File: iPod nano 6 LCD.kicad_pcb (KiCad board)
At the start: 2 copper layers, 40 x 40 mm, 49 parts, among them J1 Molex_503548-1220, J2 USB_C_Receptacle_USB2.0, J3 Conn_01x06_Male, U1 AP5724, U2. ATSAM3SD8BA-AU, U3 AZ1117-1.8, U4 TPS63001, Y1 32.768k, Y2 20MHz

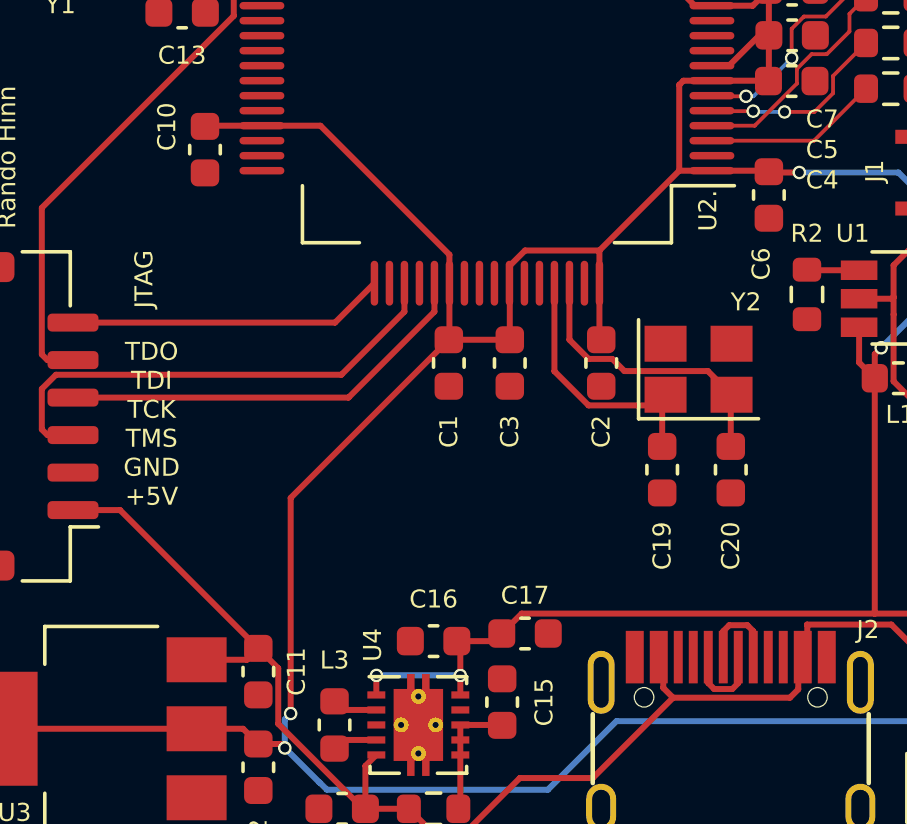
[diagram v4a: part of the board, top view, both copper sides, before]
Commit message: Add Footprint for the flash
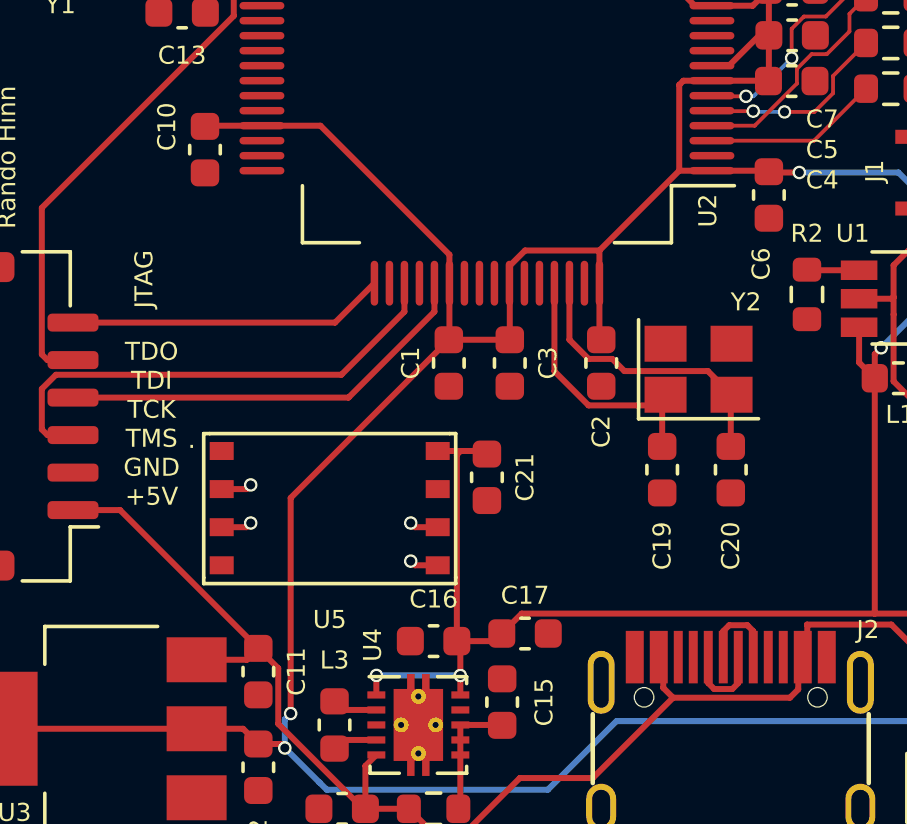
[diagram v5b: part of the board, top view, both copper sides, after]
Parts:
- added C21: 1u, Capacitor_SMD:C_0603_1608Metric, F.Cu at (137.7, 83.8)
- added U5: XTSD04GLGEAG, iPod nano 6 LCD:XTSD04GLGEAG, F.Cu at (132.4, 85.0)
- renumbered U2. to U2
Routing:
- net +3V3: track 40.9 -> 49.0 mm
- net SCLK: track 0.00 -> 1.02 mm, vias 0 -> 1
- net SD_CS: track 0.00 -> 1.02 mm, vias 0 -> 1
- net MISO: track 0.00 -> 0.96 mm, vias 0 -> 1
- net MOSI: track 0.00 -> 0.96 mm, vias 0 -> 1

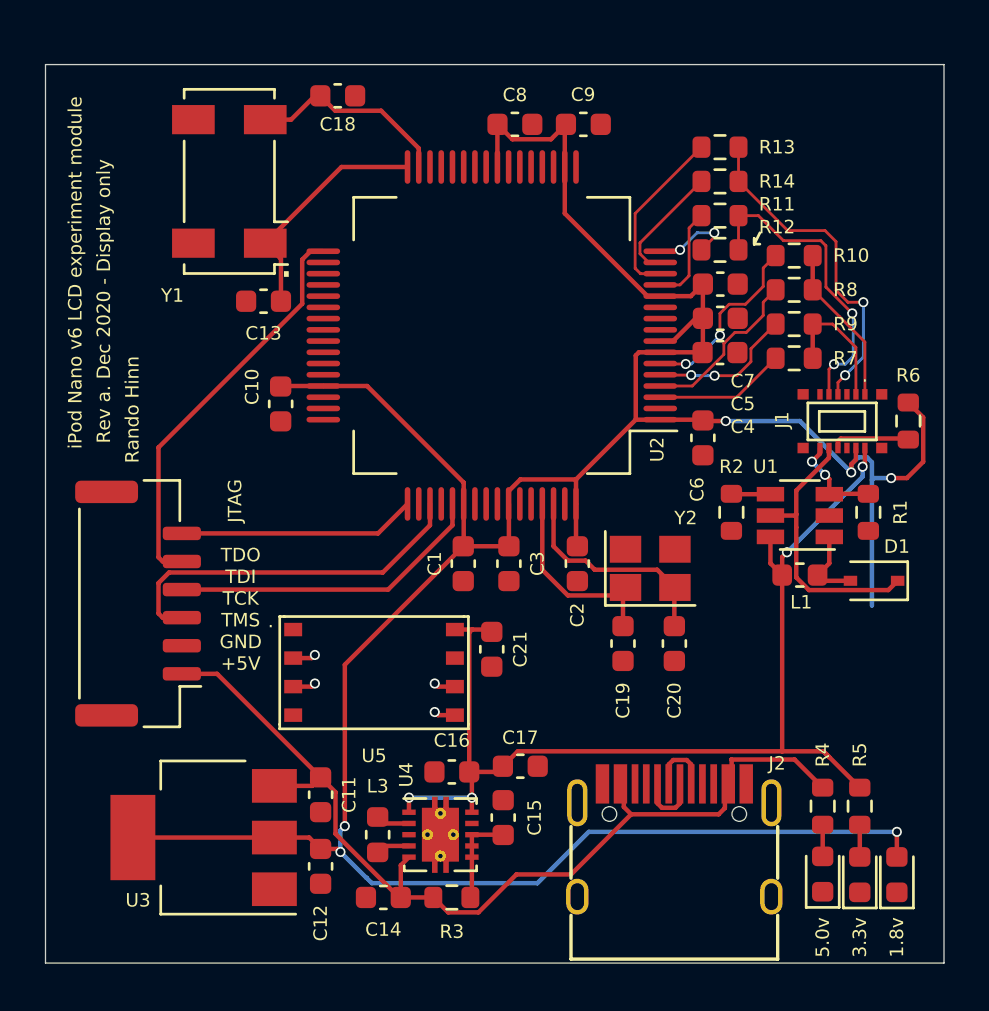
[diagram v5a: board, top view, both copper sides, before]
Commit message: Lets do some routing changes: Unroute all!
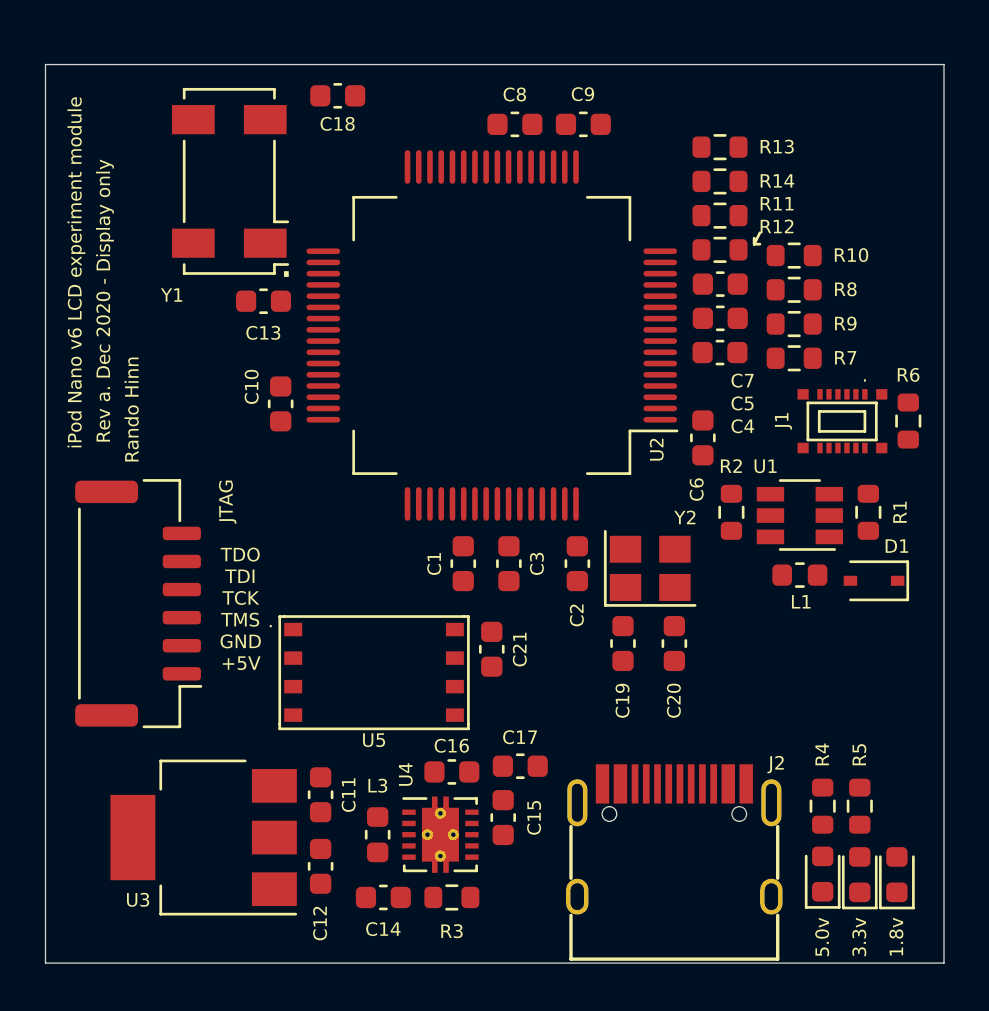
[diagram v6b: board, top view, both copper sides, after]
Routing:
- net VDDIN: track 134.4 -> 0.00 mm, vias 6 -> 0
- net +3V3: track 49.0 -> 0.00 mm, vias 4 -> 0
- net +5V: track 44.0 -> 0.00 mm
- net TDI: track 18.1 -> 0.00 mm
- net TMS: track 16.6 -> 0.00 mm
- net DP: track 15.1 -> 0.00 mm, vias 2 -> 0
- net TCK: track 14.2 -> 0.00 mm
- net DN: track 13.8 -> 0.00 mm, vias 2 -> 0
- net LED+: track 12.5 -> 0.00 mm
- net Net-(C13-Pad1): track 10.6 -> 0.00 mm
- net TDO: track 10.6 -> 0.00 mm
- net Net-(C20-Pad1): track 9.78 -> 0.00 mm
- net Net-(C18-Pad1): track 9.07 -> 0.00 mm
- net Net-(C19-Pad1): track 9.03 -> 0.00 mm
- net Net-(R10-Pad1): track 8.20 -> 0.00 mm, vias 2 -> 0
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
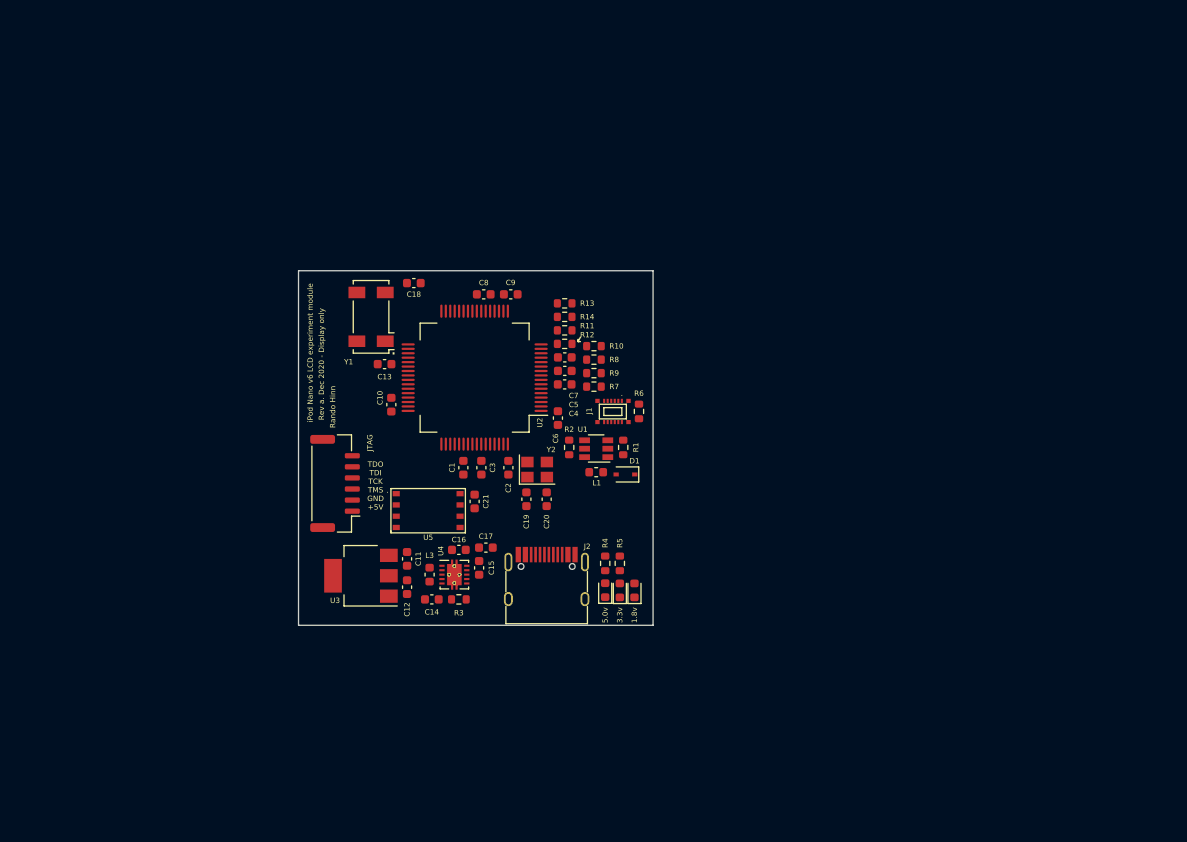
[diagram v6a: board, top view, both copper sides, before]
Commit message: Connecting up the power for the ice40 FPGA I decided to go with.
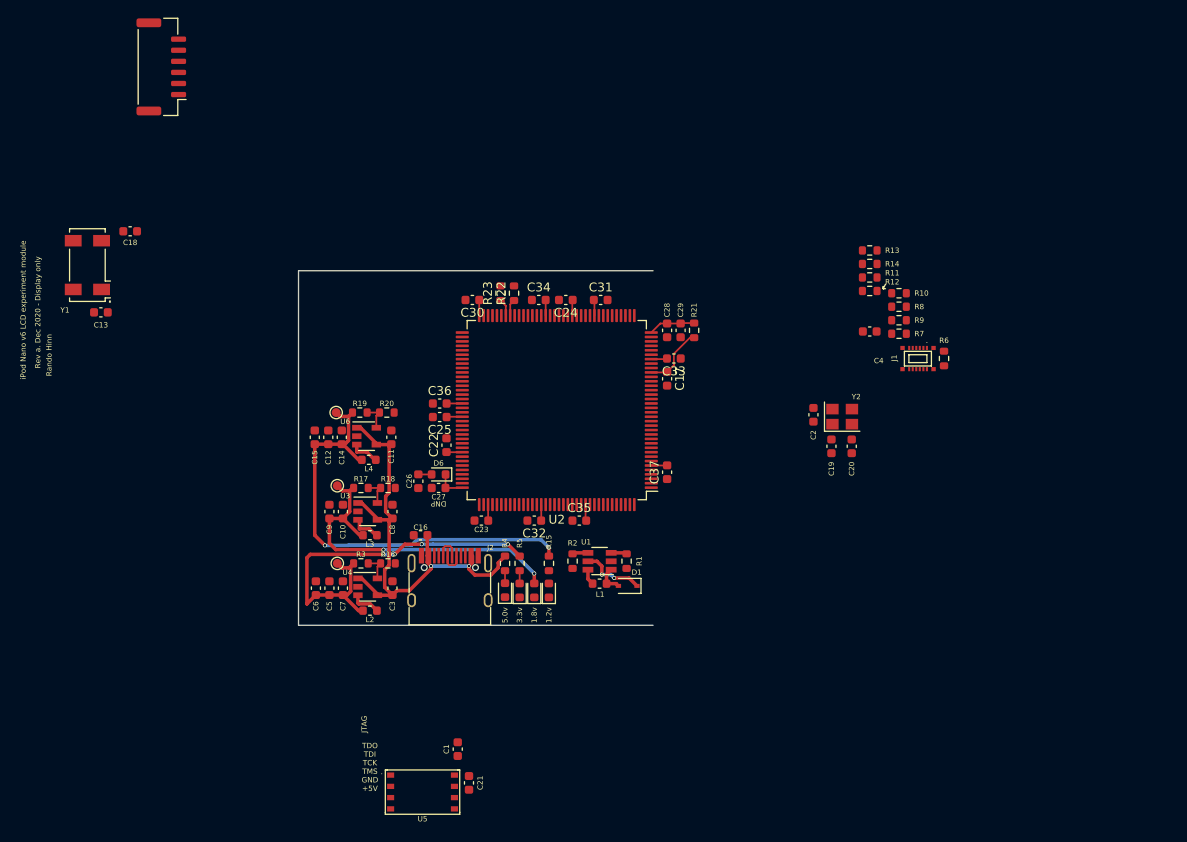
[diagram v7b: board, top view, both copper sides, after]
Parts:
- added C22: 1u, Capacitor_SMD:C_0603_1608Metric, F.Cu at (134.5, 77.5)
- added C23: 1u, Capacitor_SMD:C_0603_1608Metric, F.Cu at (138.4, 86.0)
- added C24: 1u, Capacitor_SMD:C_0603_1608Metric, F.Cu at (148.0, 61.1)
- added C25: 1u, Capacitor_SMD:C_0603_1608Metric, F.Cu at (133.7, 74.3)
- added C26: 1u, Capacitor_SMD:C_0603_1608Metric, F.Cu at (131.3, 81.5)
- added C27: DNP, Capacitor_SMD:C_0603_1608Metric, F.Cu at (133.6, 82.3)
- added C28: 10u, Capacitor_SMD:C_0603_1608Metric, F.Cu at (159.4, 64.5)
- added C29: 100n, Capacitor_SMD:C_0603_1608Metric, F.Cu at (160.9, 64.5)
- added C30: 1u, Capacitor_SMD:C_0603_1608Metric, F.Cu at (137.4, 61.1)
- added C31: 1u, Capacitor_SMD:C_0603_1608Metric, F.Cu at (151.9, 61.1)
- added C32: 1u, Capacitor_SMD:C_0603_1608Metric, F.Cu at (144.4, 86.0)
- added C33: 1u, Capacitor_SMD:C_0603_1608Metric, F.Cu at (160.1, 67.7)
- added C34: 1u, Capacitor_SMD:C_0603_1608Metric, F.Cu at (144.9, 61.1)
- added C35: 1u, Capacitor_SMD:C_0603_1608Metric, F.Cu at (149.5, 86.0)
- added C36: 1u, Capacitor_SMD:C_0603_1608Metric, F.Cu at (133.7, 72.8)
- added C37: 1u, Capacitor_SMD:C_0603_1608Metric, F.Cu at (159.4, 80.5)
- added D5: +3.3v, LED_SMD:LED_0603_1608Metric, F.Cu at (146.1, 93.9)
- added D6: ~~800mVf, Diode_SMD:D_0603_1608Metric, F.Cu at (133.6, 80.8)
- added L2: 2.2u, Inductor_SMD:L_0603_1608Metric, F.Cu at (125.9, 96.1)
- added L4: 2.2u, Inductor_SMD:L_0603_1608Metric, F.Cu at (125.7, 79.1)
- added R15: 8, Resistor_SMD:R_0603_1608Metric, F.Cu at (146.1, 90.8)
- added R16: 100k, Resistor_SMD:R_0603_1608Metric, F.Cu at (127.9, 90.8)
- added R17: 200k, Resistor_SMD:R_0603_1608Metric, F.Cu at (124.8, 82.3)
- added R18: 100k, Resistor_SMD:R_0603_1608Metric, F.Cu at (127.9, 82.3)
- added R19: 100k, Resistor_SMD:R_0603_1608Metric, F.Cu at (124.7, 73.8)
- added R20: 100k, Resistor_SMD:R_0603_1608Metric, F.Cu at (127.8, 73.8)
- added R21: 100, Resistor_SMD:R_0603_1608Metric, F.Cu at (162.4, 64.5)
- added R22: 2k2, Resistor_SMD:R_0603_1608Metric, F.Cu at (142.1, 60.3)
- added R23: 10k, Resistor_SMD:R_0603_1608Metric, F.Cu at (140.6, 60.3)
- added TP1: 1.8v, TestPoint:TestPoint_Pad_D1.0mm, F.Cu at (122.2, 82.0)
- added TP2: 3.3v, TestPoint:TestPoint_Pad_D1.0mm, F.Cu at (122.2, 90.8)
- added TP3: 1.2v, TestPoint:TestPoint_Pad_D1.0mm, F.Cu at (122.0, 73.8)
- added U6: TLV62569DBV, Package_TO_SOT_SMD:SOT-23-5, F.Cu at (125.5, 76.5)
- C10, C12, C14, C5, C6, C7, C9: value 1u -> 10u
- C11, C3, C8: value 1u -> 4.7u
- C15: value .1u -> 10u
- C17: value 10u -> 1u
- L3: value 2.2uH -> 2.2u
- R3: value 100 -> 442k
- U2: value ATSAM3SD8BA-AU -> ICE40HX1K-TQ144; footprint iPod nano 6 LCD:QFP-64_12x12_Pitch0.5mm -> Package_QFP:TQFP-144_20x20mm_P0.5mm
- U3: value AZ1117-1.8 -> TLV62569DBV; footprint Package_TO_SOT_SMD:SOT-223-3_TabPin2 -> Package_TO_SOT_SMD:SOT-23-5
- U4: value TPS63001 -> TLV62569DBV; footprint Package_SON:Texas_DRC0010J_ThermalVias -> Package_TO_SOT_SMD:SOT-23-5
- moved J3 50.9 mm to (102.3, 34.8)
- moved C5 36.1 mm to (121.3, 93.6), turned to 90 degrees
- moved C7 36.1 mm to (122.8, 93.6), turned to 90 degrees
- moved C19 34.9 mm to (177.9, 77.6)
- moved C2 34.9 mm to (175.9, 74.0)
- moved C20 34.9 mm to (180.2, 77.6)
- moved R11 34.9 mm to (182.2, 58.5)
- moved R12 34.9 mm to (182.2, 60.1)
- moved R13 34.9 mm to (182.2, 55.5)
- moved R8 34.9 mm to (185.5, 61.8)
- moved R9 34.9 mm to (185.5, 63.4)
- moved Y2 34.9 mm to (179.1, 74.2)
- moved C4 34.9 mm to (182.2, 64.6)
- moved J1 34.9 mm to (187.6, 67.7)
- moved R10 34.9 mm to (185.5, 60.3)
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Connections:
- C10 pad 1: GND -> +1V8
- C10 pad 2: VDDIN -> GND
- C12 pad 1: VDDIN -> +1V2
- C14 pad 1: +5V -> +1V2
- C15 pad 1: Net-(C15-Pad1) -> +1V2
- C16 pad 1: +3V3 -> +5V
- C17 pad 1: +3V3 -> +1V2
- C21 pad 2: +3V3 -> VDDIN
- C3 pad 1: GND -> +5V
- C3 pad 2: VDDIN -> GND
- C5 pad 1: GND -> VDDIN
- C5 pad 2: VDDIN -> GND
- C6 pad 1: GND -> VDDIN
- C6 pad 2: VDDIN -> GND
- C7 pad 1: GND -> VDDIN
- C7 pad 2: VDDIN -> GND
- C8 pad 1: GND -> +5V
- C8 pad 2: VDDIN -> GND
- C9 pad 1: GND -> +1V8
- C9 pad 2: VDDIN -> GND
- D3 pad 2: VDDIN -> +1V8
- J1 pad 2: +3V3 -> VDDIN
- J1 pad 4: VDDIN -> +1V8
- L1 pad 1: +3V3 -> VDDIN
- L3 pad 2: Net-(L3-Pad2) -> +1V8
- R3 pad 1: +5V -> VDDIN
- R3 pad 2: Net-(C15-Pad1) -> Net-(R16-Pad1)
- R5 pad 1: +3V3 -> VDDIN
- R6 pad 1: VDDIN -> +1V8
- U1 pad 6: +3V3 -> VDDIN
- U2 pad 1: VDDIN -> Net-(U2-Pad1)
- U2 pad 12: VDDIN -> Net-(U2-Pad12)
- U2 pad 13: Net-(R11-Pad1) -> GND
- U2 pad 14: Net-(R13-Pad1) -> GND
- U2 pad 15: Net-(R14-Pad1) -> Net-(U2-Pad15)
- U2 pad 16: Net-(R12-Pad1) -> Net-(U2-Pad16)
- U2 pad 17: GND -> Net-(U2-Pad17)
- U2 pad 18: VDDIN -> Net-(U2-Pad18)
- U2 pad 2: GND -> Net-(U2-Pad2)
- U2 pad 24: VDDIN -> Net-(U2-Pad24)
- U2 pad 27: Net-(U2-Pad27) -> +1V2
- U2 pad 3: IC_CLKN -> Net-(U2-Pad3)
- U2 pad 30: Net-(U2-Pad30) -> +1V8
- U2 pad 31: Net-(C18-Pad1) -> Net-(U2-Pad31)
- U2 pad 32: Net-(C13-Pad1) -> Net-(U2-Pad32)
- U2 pad 33: TDI -> Net-(U2-Pad33)
- U2 pad 35: Net-(U2-Pad35) -> GNDPLL
- U2 pad 36: Net-(U2-Pad36) -> VCCPLL
- U2 pad 4: IC_CLKP -> Net-(U2-Pad4)
- U2 pad 45: VDDIN -> Net-(U2-Pad45)
- U2 pad 46: GND -> VDDIN
- U2 pad 49: TDO -> Net-(U2-Pad49)
- U2 pad 5: Net-(R9-Pad1) -> GND
- U2 pad 51: TMS -> +1V2
- U2 pad 53: TCK -> Net-(U2-Pad53)
- U2 pad 54: VDDIN -> Net-(U2-Pad54)
- U2 pad 57: Net-(U2-Pad57) -> VDDIN
- U2 pad 58: VDDIN -> Net-(U2-Pad58)
- U2 pad 59: Net-(U2-Pad59) -> GND
- U2 pad 6: Net-(R10-Pad1) -> +1V8
- U2 pad 60: GND -> Net-(U2-Pad60)
- U2 pad 61: Net-(C19-Pad1) -> Net-(U2-Pad61)
- U2 pad 62: Net-(C20-Pad1) -> Net-(U2-Pad62)
- U2 pad 64: VDDIN -> Net-(U2-Pad64)
- U2 pad 7: VDDIN -> Net-(U2-Pad7)
- U2 pad 8: VDDIN -> Net-(U2-Pad8)
- U3 pad 1: GND -> +5V
- U3 pad 2: VDDIN -> GND
- U3 pad 3: +5V -> Net-(L3-Pad1)
- U4 pad 1: +3V3 -> +5V
- U4 pad 2: Net-(L3-Pad2) -> GND
- U4 pad 3: GND -> Net-(L2-Pad1)
- U4 pad 4: Net-(L3-Pad1) -> +5V
- U4 pad 5: +5V -> Net-(R16-Pad1)
- U5 pad 8: +3V3 -> VDDIN
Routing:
- net +1V2: track 0.00 -> 63.0 mm, vias 0 -> 2
- net VDDIN: track 0.00 -> 56.2 mm, vias 0 -> 4
- net +5V: track 0.00 -> 53.8 mm, vias 0 -> 2
- net +1V8: track 0.00 -> 45.9 mm, vias 0 -> 2
- net LED+: track 0.00 -> 7.24 mm, vias 0 -> 2
- net VCCPLL: track 0.00 -> 5.28 mm
- net VPP_2V5: track 0.00 -> 3.44 mm
- net Net-(L3-Pad1): track 0.00 -> 3.41 mm
- net Net-(L2-Pad1): track 0.00 -> 3.38 mm
- net Net-(R17-Pad2): track 0.00 -> 3.37 mm
- net Net-(R19-Pad2): track 0.00 -> 3.26 mm
- net Net-(R16-Pad1): track 0.00 -> 3.24 mm
- net Net-(D1-Pad2): track 0.00 -> 3.23 mm
- net Net-(L4-Pad1): track 0.00 -> 3.21 mm
- net Net-(J2-PadA7): track 0.00 -> 2.89 mm
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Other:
- board text added: "1.2v"
- board text added: "DNP"

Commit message: Add config SPI and silkscreen for lcd
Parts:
- removed C13, C18: 12.5p, Capacitor_SMD:C_0603_1608Metric
- removed C19, C20: 10p, Capacitor_SMD:C_0603_1608Metric
- removed Y1: 32.768k, Crystal:Crystal_SMD_Abracon_ABS25-4Pin_8.0x3.8mm
- removed Y2: 20MHz, Crystal:Crystal_SMD_Abracon_ABM8G-4Pin_3.2x2.5mm
- added C38: 1u, Capacitor_SMD:C_0603_1608Metric, F.Cu at (132.8, 60.5)
- added U7: AT25xxx, Package_DFN_QFN:DFN-8-1EP_3x2mm_P0.5mm_EP1.75x1.45mm, F.Cu at (132.2, 62.6)
- moved J1 13.2 mm to (175.0, 63.8), turned to 270 degrees
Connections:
- U2 pad 67: Net-(U2-Pad67) -> MOSI
- U2 pad 68: Net-(U2-Pad68) -> MISO
- U2 pad 70: Net-(U2-Pad70) -> SCK
- U2 pad 71: Net-(U2-Pad71) -> CFG_CS
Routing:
- net VDDIN: track 56.2 -> 71.6 mm, vias 4 -> 5
- net MISO: track 0.00 -> 13.1 mm, vias 0 -> 2
- net CFG_CS: track 0.00 -> 12.9 mm, vias 0 -> 2
- net MOSI: track 0.00 -> 9.12 mm
- net LED+: track 7.24 -> 16.1 mm
- net LED-: track 1.78 -> 9.11 mm
- net SCK: track 0.00 -> 7.32 mm
